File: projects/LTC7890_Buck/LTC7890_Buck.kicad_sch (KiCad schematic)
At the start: 94 parts, among them J1 Bat In, J2 24V Out, J3 I2C Socket, J4 I2C Socket, Q1 IGC025S08S1, Q2 IGC025S08S1, Q3 IGC025S08S1, Q4 IGC025S08S1, SW1 Addr_Switch, SW2 Addr_Switch, U1 LTC7890, U2 TLV74033, U3 INA226

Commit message: Finished PCB
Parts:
- added C16, C17, C26, C27, C31, C42: 100nF, Capacitor_SMD:C_0603_1608Metric, symbol Device:C
- added NT1: NetTie_2, footprints:NetTie-2_SMD_Pad0.25mm, symbol Device:NetTie_2
- R14, R7: value 47 -> 100
- R15, R19, R3, R5: value 0 -> 1
- U3: footprint Package_SO:VSSOP-10_3x3mm_P0.5mm -> Package_SO:TSSOP-10_3x3mm_P0.5mm
- renumbered C19 to C18, C20 to C19, C21 to C20, C22 to C21, C23 to C22, C24 to C23, C25 to C24, C26 to C25, C16 to C28, C17 to C29, C18 to C30, C27 to C32, C28 to C33, C29 to C34, C30 to C35, C31 to C36, C32 to C37, C33 to C38, C34 to C39, C35 to C40, C36 to C41, C37 to C43, C38 to C44, R18 to R17, R17 to R18
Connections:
- net +24V: no longer U1.26 (EXTVCC)
- net VDD: now also C16.2, C17.2, C26.2, C27.2, C31.1
- net VOUT: now also U1.26 (EXTVCC), C42.2
- net at L1.1, Q1.3 (S), Q1.5 (S)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: no longer C32.1, Q1.6 (SS), U1.31 (SW1)
- net at L2.2, Q3.3 (S), Q3.5 (S)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: no longer C39.1, Q3.6 (SS), U1.20 (SW2)
- net GND renamed GNDPWR
- net GNDPWR: now also C16.1, C17.1, C26.1, C27.1, C31.2, C42.1, NT1.2; no longer C36.1, C37.2, C38.2, C40.2, C41.2, C43.1, D1.1 (K), J3.2 (Pin_2), J4.2 (Pin_2), R16.2, R2.1, R9.1, SW1.1, SW2.1, U1.14 (ITH2), U1.15 (SS2), U1.3 (PLLIN), U1.6 (GND), U1.7 (DRVUV), U1.8 (DRVSET), U2.2 (GND), U3.7 (GND)
- new net: C32.1, Q1.6 (SS), U1.31 (SW1)
- new net: C39.1, Q3.6 (SS), U1.20 (SW2)
- new net GNDA: C36.1, C37.2, C38.2, C40.2, C41.2, C43.1, D1.1 (K), J3.2 (Pin_2), J4.2 (Pin_2), NT1.1, R16.2, R2.1, R9.1, SW1.1, SW2.1, U1.14 (ITH2), U1.15 (SS2), U1.3 (PLLIN), U1.6 (GND), U1.8 (DRVSET), U2.2 (GND), U3.7 (GND)
- no-connect marks 4 -> 5
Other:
- moved on the sheet: C18, C19, C20, C21, C22, C23, C24, C25, C36, C37, C38, R18

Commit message: Minor changes 2
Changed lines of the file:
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@@
 		(property "Voltage" "50V"
 			(at 44.45 26.4161 0)
-			(hide yes)
 			(show_name no)
 			(do_not_autoplace no)

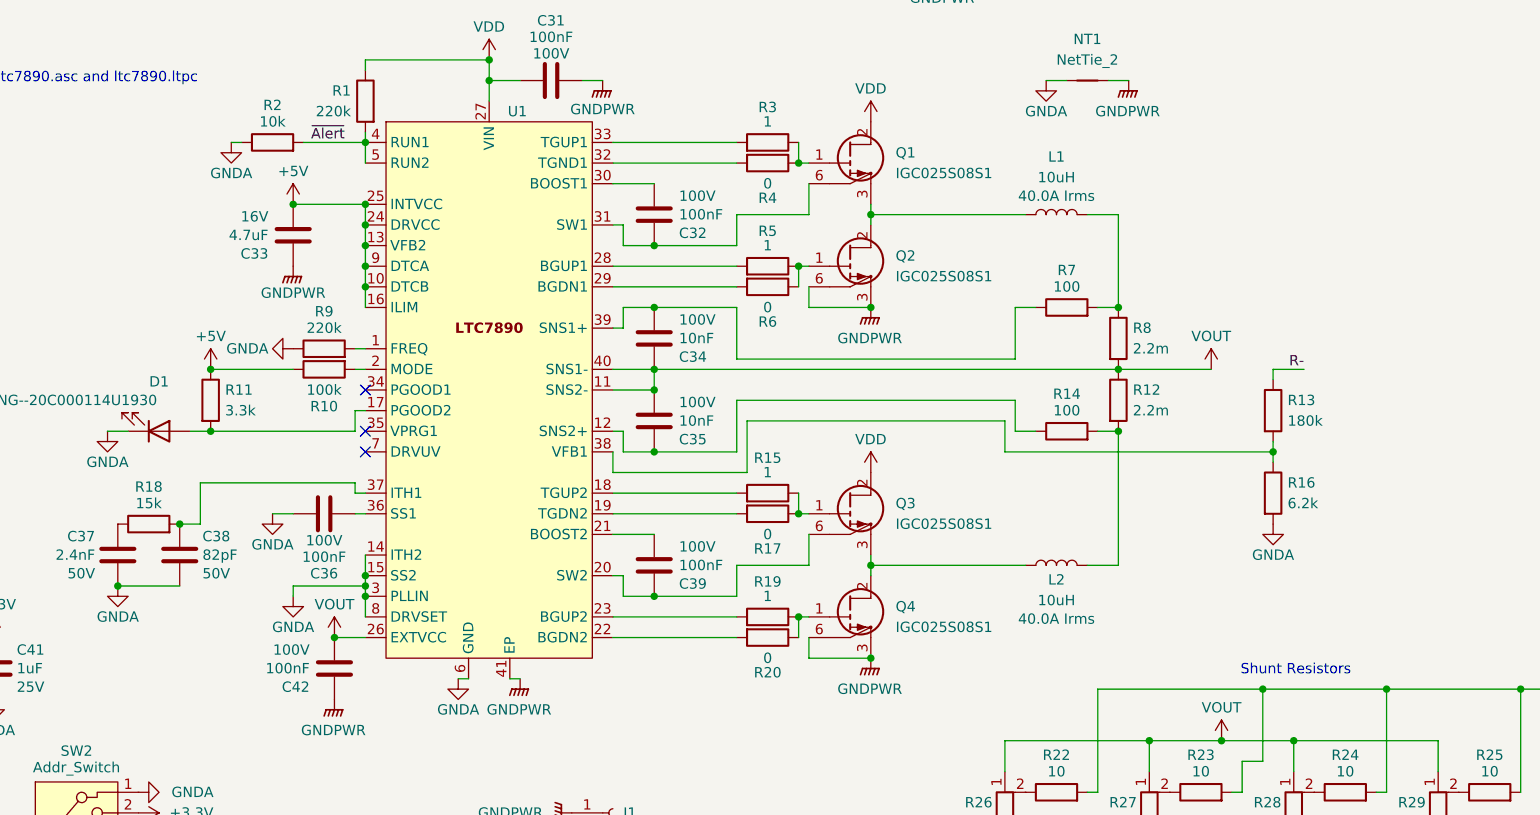
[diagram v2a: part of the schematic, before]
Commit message: Added low side fet diode
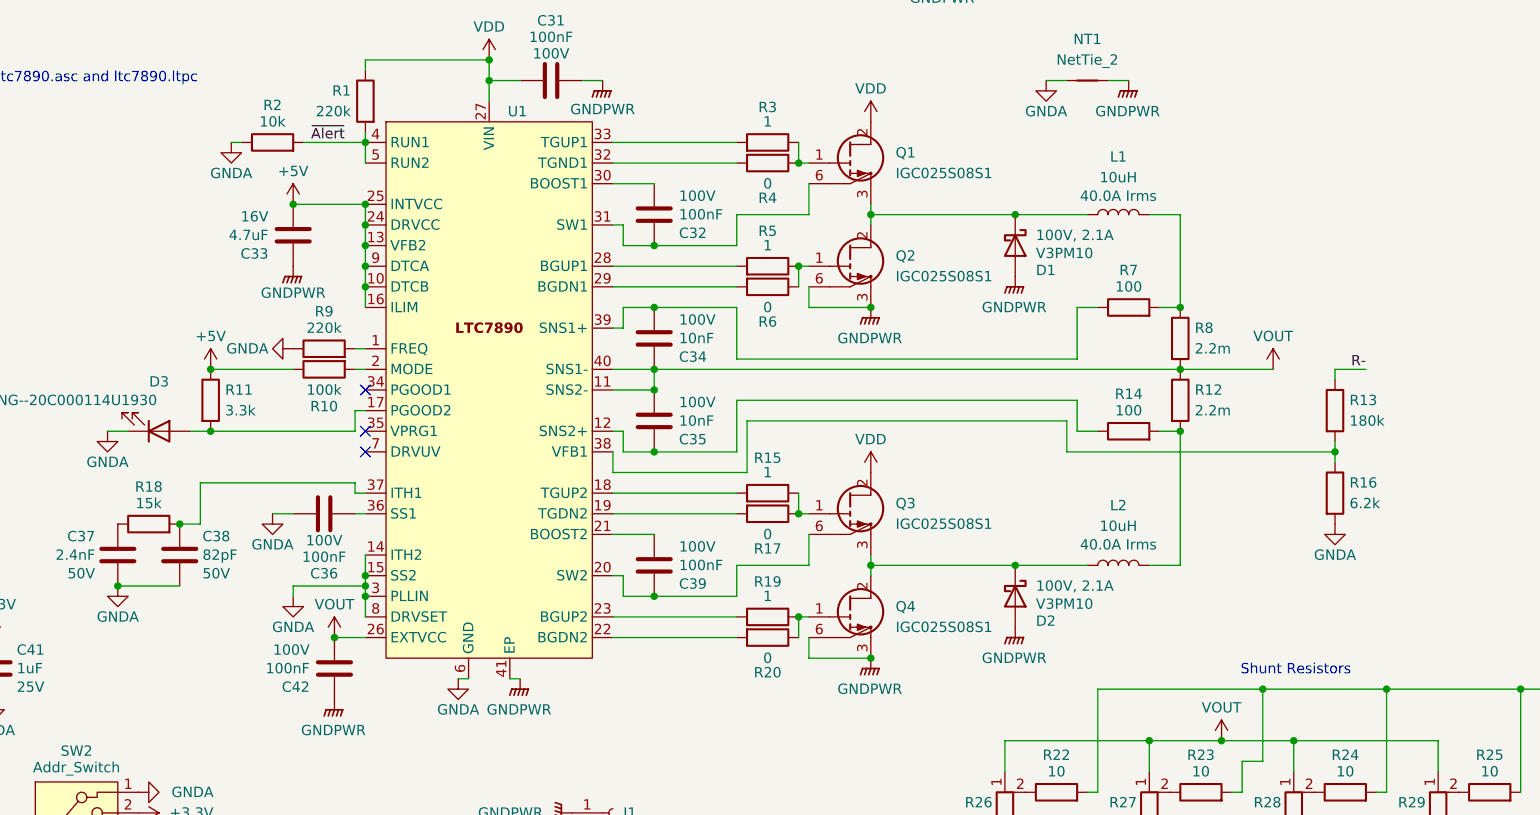
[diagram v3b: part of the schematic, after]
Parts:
- added D1, D2: V3PM10, footprints:D_SMP_DO-220AA, symbol Device:D_Schottky
- renumbered D1 to D3
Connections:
- net GNDPWR: now also D1.2 (A), D2.2 (A)
- net at L2.2, Q3.3 (S), Q3.5 (S)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: now also D2.1 (K)
- net at L1.1, Q1.3 (S), Q1.5 (S)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: now also D1.1 (K)
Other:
- moved on the sheet: L1, L2, R12, R13, R14, R16, R7, R8

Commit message: Minor changes again
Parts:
- R15, R3: value 1 -> 2.2
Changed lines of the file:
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@@
 			)
 		)
-		(property "Value" "1"
+		(property "Value" "2.2"
 			(at 149.86 63.5 90)
 			(show_name no)
@@
 			)
 		)
-		(property "Datasheet" "https://www.lcsc.com/product-detail/C112305.html"
+		(property "Datasheet" "https://www.lcsc.com/product-detail/C112307.html"
 			(at 149.86 66.04 0)
 			(hide yes)
@@
 			)
 		)
-		(property "Value" "1"
+		(property "Value" "2.2"
 			(at 149.86 106.68 90)
 			(show_name no)
@@
 			)
 		)
-		(property "Datasheet" "https://www.lcsc.com/product-detail/C112305.html"
+		(property "Datasheet" "https://www.lcsc.com/product-detail/C112307.html"
 			(at 149.86 109.22 0)
 			(hide yes)

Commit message: New Revision
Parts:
- removed TP3, TP4: TestPoint, TestPoint:TestPoint_Keystone_5000-5004_Miniature, symbol Connector:TestPoint
- removed TP5: TestPoint, TestPoint:TestPoint_Pad_D2.0mm, symbol Connector:TestPoint
- added C32, C33: 100nF, Capacitor_SMD:C_0603_1608Metric, symbol Device:C
- added H1, H2, H3, H4: MountingHole, MountingHole:MountingHole_3.2mm_M3, symbol Mechanical:MountingHole
- added M1: AUB0524VHD, symbol Motor:Fan
- added Q5: GSF3400, Package_TO_SOT_SMD:SOT-23, symbol Transistor_FET:Q_NMOS_GSD
- added R38: 8.2k, Resistor_SMD:R_0603_1608Metric, symbol Device:R
- added R5, R6: 10k, Resistor_SMD:R_0603_1608Metric, symbol Device:R
- added SW3, SW4: SW_SP3T, footprints:CL-SB-13A, symbol Switch:SW_SP3T
- added TH1: JSNB103F344FBEWH, Resistor_SMD:R_0603_1608Metric, symbol Device:Thermistor
- added U2: ADC101C021CIMM, Package_SO:MSOP-8_3x3mm_P0.65mm, symbol Analog_ADC:ADC101C021CIMM
- R36: renamed from R34; now not fitted
- R37: renamed from R35; now not fitted
- SW1, SW2: value Addr_Switch -> SW_SP4T
- TP1, TP2: footprint TestPoint:TestPoint_Keystone_5000-5004_Miniature -> TestPoint:TestPoint_THTPad_D2.0mm_Drill1.0mm
- renumbered C32 to C34, C33 to C35, C34 to C36, C35 to C37, C36 to C38, C37 to C39, C38 to C40, C39 to C41, C40 to C42, C41 to C43, C42 to C44, C43 to C45, C44 to C46, R8 to R10, R9 to R11, R10 to R12, R11 to R13, R12 to R14, R13 to R15, R14 to R16, R15 to R17, R16 to R18, R17 to R19, R18 to R20, R19 to R21, R20 to R22, R21 to R23, R22 to R24, R23 to R25, R24 to R26, R25 to R27, R26 to R28, R27 to R29, R28 to R30, R29 to R31, R30 to R32, R31 to R33, R32 to R34, R33 to R35, R5 to R7, R6 to R8, R7 to R9, U2 to U3, U3 to U4
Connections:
- net +3.3V: now also C33.2, R6.1, SW3.1, SW4.1, TH1.1, U2.5 (VA)
- net GNDA: now also C32.1, C33.1, R5.2, SW3.4, SW4.4, U2.7 (GND)
- net GNDPWR: now also J1.2 (Pin_2), Q5.2 (S); no longer J1.1 (Pin_1), TP2.1
- net VDD: now also J1.1 (Pin_1); no longer J1.2 (Pin_2), TP1.1
- net VOUT: now also TP1.1, M1.1 (+)
- net ~{Alert}: now also R38.2; no longer U4.3 (~{Alert})
- net SDA: now reaches J3.3 (Pin_3), J4.3 (Pin_3), R36.2, SW1.3, SW2.3, U4.4 (SDA)
- net SDA: now also U2.8 (SDA)
- net SCL: now reaches J3.4 (Pin_4), J4.4 (Pin_4), R37.2, SW1.4, SW2.4, U4.5 (SCL)
- net SCL: now also U2.1 (SCL)
- net at D3.2 (A), R13.2: now also U1.34 (PGOOD1); no longer U1.17 (PGOOD2)
- new net: SW4.3, U2.6 (ADR1)
- new net: M1.2 (-), Q5.3 (D), TP2.1
- new net: C32.2, R5.1, TH1.2, U2.4 (VIN)
- new net: R38.1, U4.3 (~{Alert})
- new net: Q5.1 (G), R6.2, U2.2 (ALERT)
- new net: SW3.3, U2.3 (ADR0)
- no-connect marks 5 -> 7
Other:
- note added: "Fan Control"
- note removed: "24V Feedback"
- title: LM5143 Buck -> LTC7890 Buck
- moved on the sheet: C31, C34, C35, C36, C37, C38, C39, C40, C41, C44, D1, D2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

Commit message: Minor changes
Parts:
- added D4: V3PM10, footprints:D_SMP_DO-220AA, symbol Device:D_Schottky
- Q5: value GSF3400 -> PJA3438
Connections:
- net +3.3V: now also R6.2; no longer R6.1
- net VOUT: now also D4.1 (K)
- net at M1.2 (-), Q5.3 (D), TP2.1: now also D4.2 (A)
- net at Q5.1 (G), U2.2 (ALERT): now also R6.1; no longer R6.2
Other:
- moved on the sheet: M1, Q5, TP1, TP2

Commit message: Minor rewiring
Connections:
- net +3.3V: now also SW3.4, SW4.4; no longer SW3.1, SW4.1
- net GNDA: now also SW3.2, SW4.2; no longer SW3.4, SW4.4
